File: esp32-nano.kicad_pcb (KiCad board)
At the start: 2 copper layers, 52.8 x 21.3 mm, 46 parts, among them K1 SW_MEC_5E, K2 SW_MEC_5E, P2 Conn_01x12, P3 Conn_01x18, U1 CP2102N-A01-GQFN28, U2 ME6211C33M5G, U3 MPU-6050, U4 ESP32PICO_D4, U5 OLED-12880

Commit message: .
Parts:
- A1: footprint CA-C03:CA-C03 -> Antenna:CA-C03
- K1, K2: footprint SKSCLCE010:SKSCLCE010 -> Button:SKSC_NO_HOLE
- U4: footprint ESP32_PICO_D4:ESP32_PICO_D4 -> SOC:ESP32_PICO_D4

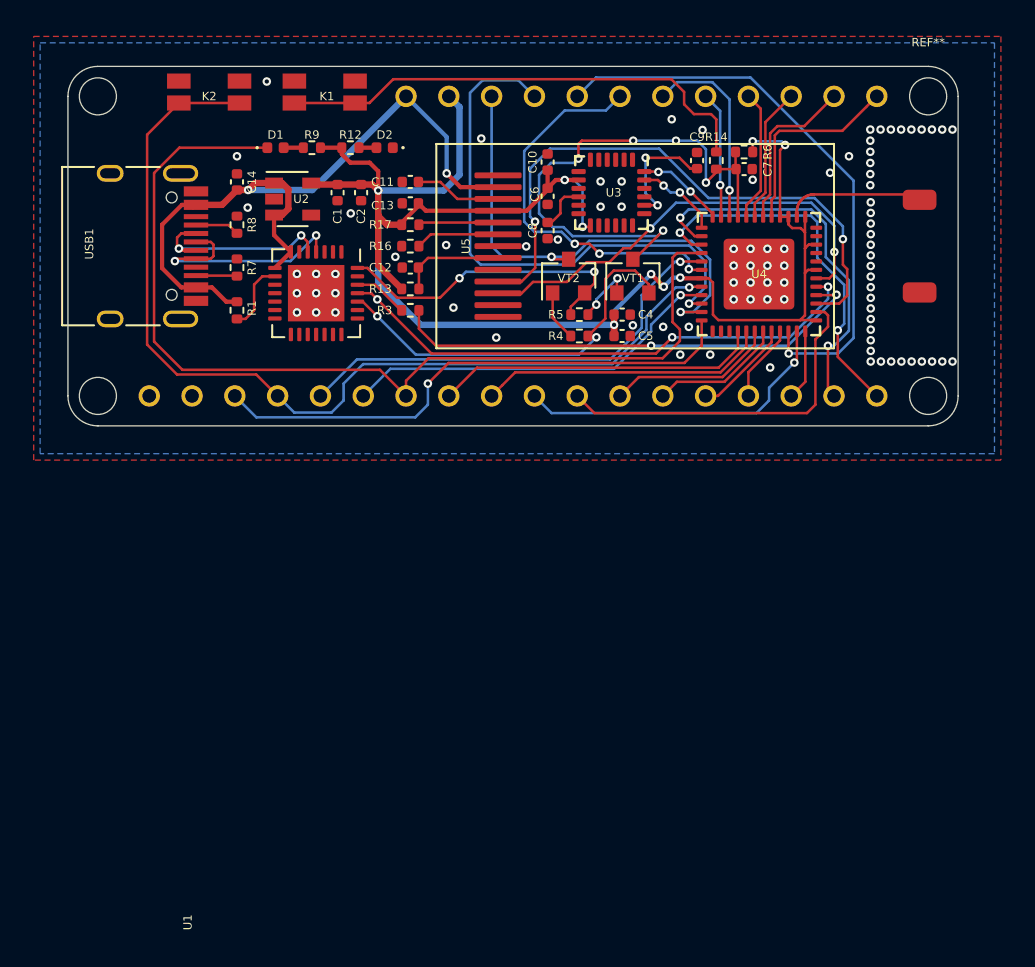
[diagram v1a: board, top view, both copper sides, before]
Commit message: 引出psram
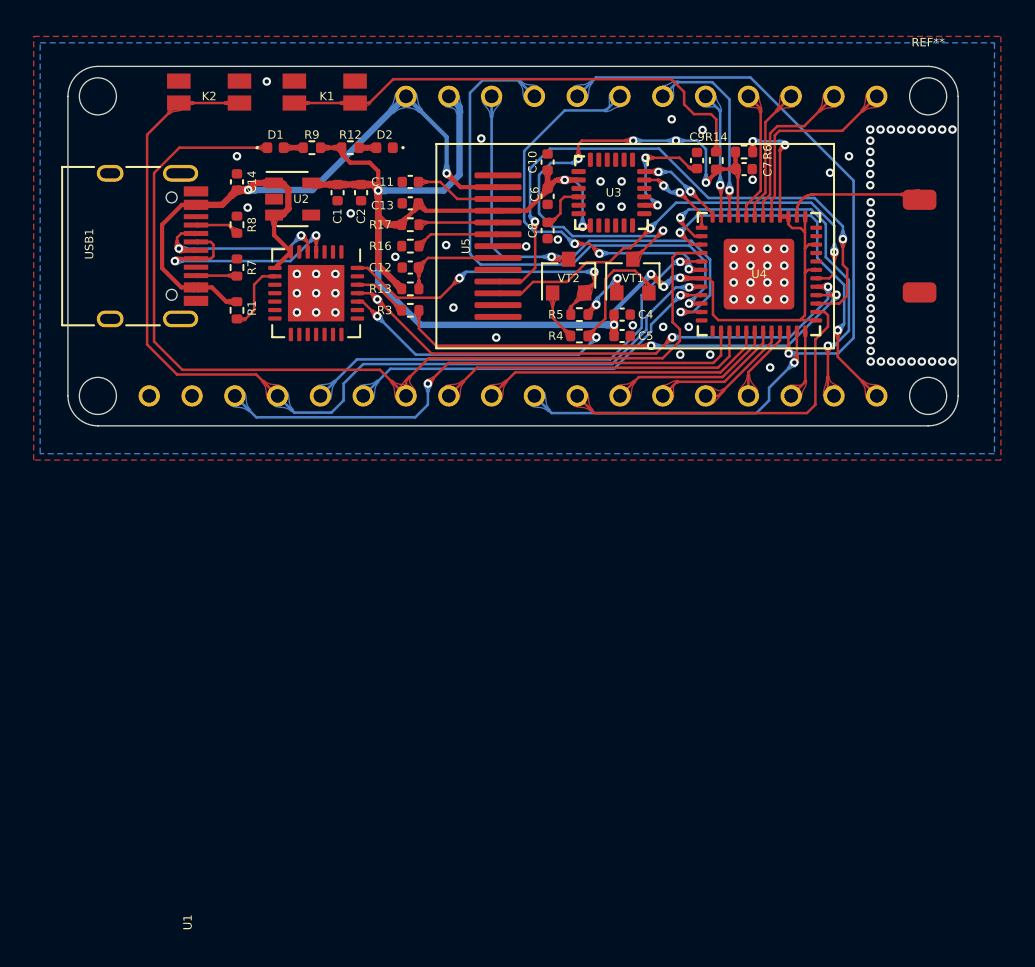
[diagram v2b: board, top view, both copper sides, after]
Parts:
- R14: value 1K -> 0R
- R9: value 10K -> 3K
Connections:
- net FLASH_CS renamed Net-(U4-Pad25)
- P3 pad 16: GPIO4 -> VDD_SIO
- U4 pad 24: GPIO4 -> Net-(U4-Pad24)
- U4 pad 26: Net-(U4-Pad26) -> VDD_SIO
- U4 pad 27: FLASH_SD0 -> GPIO9
- U4 pad 28: GPIO9 -> Net-(U4-Pad28)
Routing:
- net VDD_SIO: track 0.00 -> 33.1 mm, vias 0 -> 1
- net GPIO4: track 32.2 -> 0.00 mm, vias 1 -> 0

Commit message: .
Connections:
- net GPIO9 renamed GPIO17
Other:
- board text added: "17"
- board text added: "JLCJLCJLCJLC"
- board text added: "KEY"
- board text added: "VSIO"
- board text removed: "4"
- board text removed: "9"
- board text removed: "BTN"
